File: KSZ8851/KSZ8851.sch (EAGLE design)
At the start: 53 parts, among them IC1 AT93C46A-10SQ-2.7, P1 RB1-125BAG1A

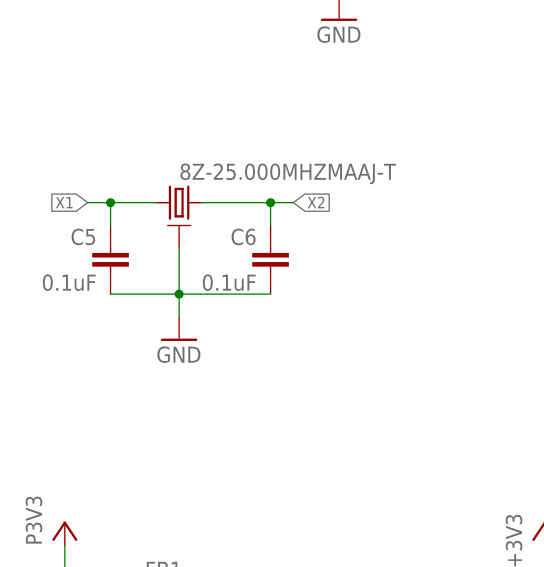
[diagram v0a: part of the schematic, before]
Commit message: Fix angle wire angle and add power LED
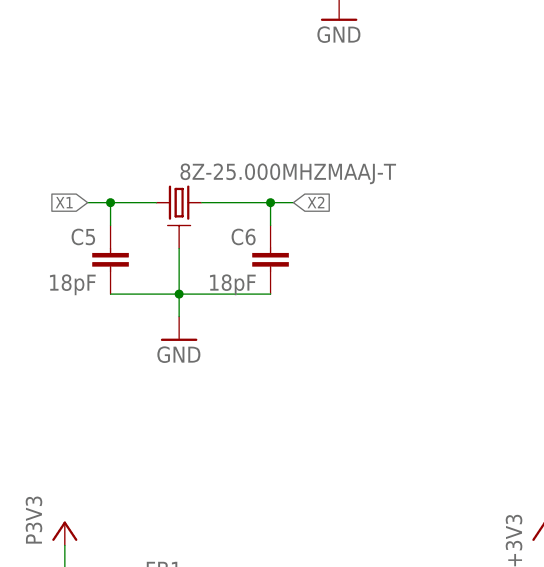
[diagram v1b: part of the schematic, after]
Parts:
- C5, C6: value 0.1uF -> 18pF
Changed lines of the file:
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@@
 <part name="+3V5" library="supply1" deviceset="+3V3" device=""/>
 <part name="-25.000MHZMAAJ-T1" library="crystal" deviceset="8Z" device="" technology="-25.000MHZMAAJ-T"/>
-<part name="C5" library="rcl" deviceset="C-EU" device="C0603" value="0.1uF"/>
-<part name="C6" library="rcl" deviceset="C-EU" device="C0603" value="0.1uF"/>
+<part name="C5" library="rcl" deviceset="C-EU" device="C0603" value="18pF"/>
+<part name="C6" library="rcl" deviceset="C-EU" device="C0603" value="18pF"/>
 <part name="GND7" library="supply1" deviceset="GND" device=""/>
 <part name="JP1" library="pinhead" deviceset="PINHD-2X5" device=""/>

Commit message: Generate gerber file
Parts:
- added LED1: Green, led:LEDSML0603
- added R13: 1.5k, rcl:R-EU_R0603
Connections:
- new net N$4: LED1.A, R13.2
- net +3V3: now also R13.1
- net GND: now also LED1.C
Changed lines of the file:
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@@
 <part name="SJ4" library="jumper" deviceset="SJ" device=""/>
 <part name="GND15" library="supply1" deviceset="GND" device=""/>
+<part name="LED1" library="led" deviceset="LED" device="SML0603" value="Green"/>
+<part name="R13" library="rcl" deviceset="R-EU_" device="R0603" value="1.5k"/>
 </parts>
 <sheets>
@@
 <instance part="SJ4" gate="1" x="342.9" y="43.18" rot="R90"/>
 <instance part="GND15" gate="1" x="335.28" y="48.26"/>
+<instance part="LED1" gate="G$1" x="76.2" y="96.52"/>
+<instance part="R13" gate="G$1" x="76.2" y="106.68" rot="R270"/>
 </instances>
 <busses>
@@
 <wire x1="66.04" y1="93.98" x2="66.04" y2="91.44" width="0.1524" layer="91"/>
 <junction x="66.04" y="93.98"/>
+<pinref part="LED1" gate="G$1" pin="C"/>
+<wire x1="76.2" y1="91.44" x2="66.04" y2="91.44" width="0.1524" layer="91"/>
+<junction x="66.04" y="91.44"/>
 </segment>
 <segment>
@@
 <wire x1="40.64" y1="109.22" x2="55.88" y2="109.22" width="0.1524" layer="91"/>
 <wire x1="55.88" y1="109.22" x2="66.04" y2="109.22" width="0.1524" layer="91"/>
-<wire x1="66.04" y1="109.22" x2="66.04" y2="114.3" width="0.1524" layer="91"/>
+<wire x1="66.04" y1="109.22" x2="66.04" y2="111.76" width="0.1524" layer="91"/>
 <pinref part="C10" gate="G$1" pin="1"/>
+<wire x1="66.04" y1="111.76" x2="66.04" y2="114.3" width="0.1524" layer="91"/>
 <wire x1="66.04" y1="101.6" x2="66.04" y2="109.22" width="0.1524" layer="91"/>
 <junction x="66.04" y="109.22"/>
@@
 <wire x1="40.64" y1="101.6" x2="40.64" y2="109.22" width="0.1524" layer="91"/>
 <junction x="40.64" y="109.22"/>
+<pinref part="R13" gate="G$1" pin="1"/>
+<wire x1="66.04" y1="111.76" x2="76.2" y2="111.76" width="0.1524" layer="91"/>
+<junction x="66.04" y="111.76"/>
 </segment>
 </net>
@@
 </segment>
 </net>
+<net name="N$4" class="0">
+<segment>
+<pinref part="R13" gate="G$1" pin="2"/>
+<pinref part="LED1" gate="G$1" pin="A"/>
+<wire x1="76.2" y1="101.6" x2="76.2" y2="99.06" width="0.1524" layer="91"/>
+</segment>
+</net>

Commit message: Add Exmachina logo and CC
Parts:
- added U$2: EXMACHINA-LOGO-NAME, exmachina:EXMACHINA-LOGO-NAME
- added U$3: CC-BY-SA, cc-by-sa:CC-BY-SA
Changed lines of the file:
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@@
 <part name="LED1" library="led" deviceset="LED" device="SML0603" value="Green"/>
 <part name="R13" library="rcl" deviceset="R-EU_" device="R0603" value="1.5k"/>
+<part name="U$2" library="exmachina" deviceset="EXMACHINA-LOGO" device="-NAME"/>
+<part name="U$3" library="cc-by-sa" deviceset="CC-BY-SA" device=""/>
 </parts>
 <sheets>
@@
 <instance part="LED1" gate="G$1" x="76.2" y="96.52"/>
 <instance part="R13" gate="G$1" x="76.2" y="106.68" rot="R270"/>
+<instance part="U$2" gate="G$1" x="311.15" y="19.05"/>
+<instance part="U$3" gate="A" x="303.53" y="8.89"/>
 </instances>
 <busses>

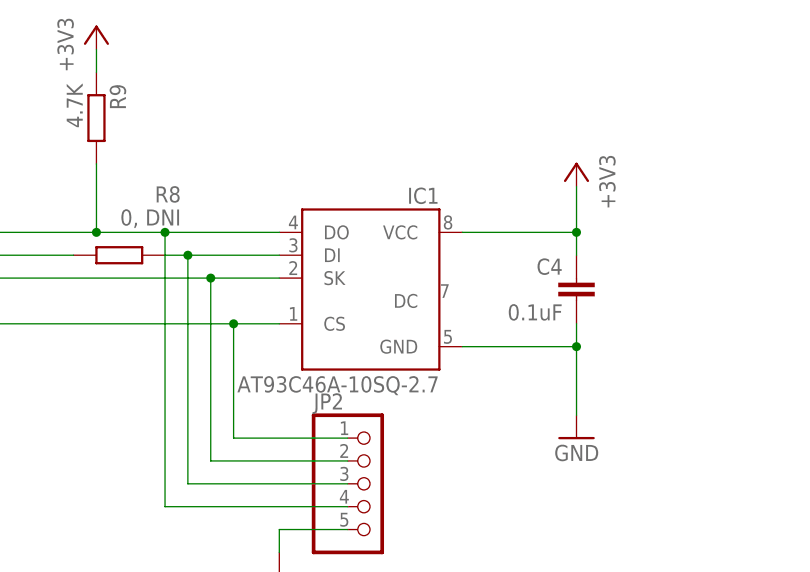
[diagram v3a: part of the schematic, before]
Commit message: Add BOM to KSZ8851 board and place component name on the board
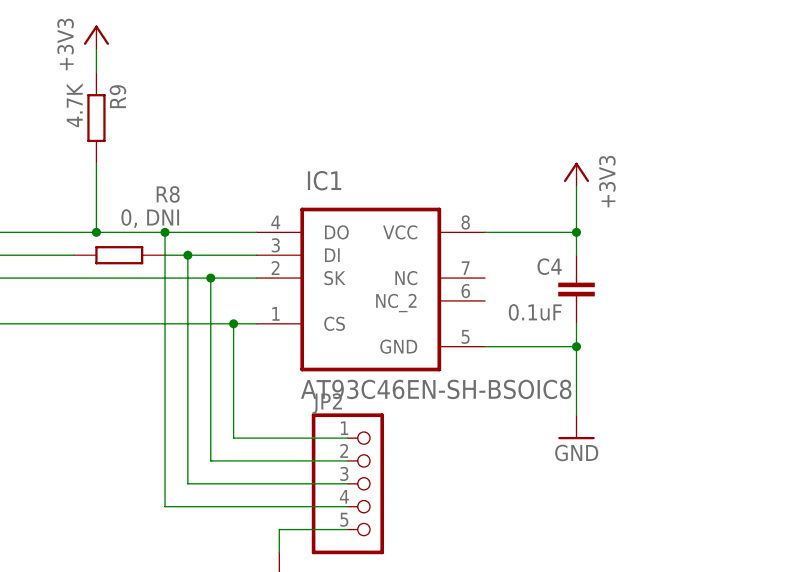
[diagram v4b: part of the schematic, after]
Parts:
- -25.000MHZMAAJ-T1: MPN (none) -> 8Z-25.000MAAJ-T; OC_NEWARK (none) -> 84R5794
- C1, C10, C13, C14, C2, C4, C9: MPN (none) -> MC0603B104K160CT; OC_NEWARK (none) -> 06R4923
- C11, C12, C3, C7, C8: MPN (none) -> MCCTA475M010; OC_NEWARK (none) -> 01M8221
- C5, C6: MPN (none) -> MC0603N180J500CT; OC_NEWARK (none) -> 06R5138
- FB1, FB2: OC_NEWARK (none) -> 66W8861
- IC1: value AT93C46A-10SQ-2.7 -> AT93C46EN-SH-BSOIC8; device atmel:AT93C46A-10SQ-2.7 -> atmel:AT93C46EN-SH-BSOIC8; MPN (none) -> AT93C46EN-SH-T; OC_NEWARK (none) -> 68T5247
- JP1: MPN (none) -> M20-9980546; OC_NEWARK (none) -> 84K8708
- JP2: MF (none) -> FARNELL; MPN (none) -> M22-2010505; OC_NEWARK (none) -> 08WX6673
- JP3, JP4, JP5, JP6, MP1, MP2, MP3, MP4, P1, SJ1, SJ2, SJ3, SJ4, TP1, TP2, TP3, TP4, TP5, TP6, TP7, U$2, U$3: OC_NEWARK (none) -> unknown
- LED1: MPN (none) -> OVS-0604; OC_NEWARK (none) -> 15R2206
- R1: MPN (none) -> MC0063W060313K01; OC_NEWARK (none) -> 94W5780
- R10, R11, R12, R9: MF (none) -> Multicomp Passives; MPN (none) -> MC0063W060314K7; OC_NEWARK (none) -> 58K4608
- R13: MPN (none) -> MCMR06X1501FTL; OC_NEWARK (none) -> 86T3542
- R2, R3, R4, R5: MPN (none) -> MC0603SAF499JT5E; OC_NEWARK (none) -> 79M5983
- R6, R7: MF (none) -> Multicomp Passives; MPN (none) -> MC0063W06031220R; OC_NEWARK (none) -> 58K4526
- R8: MF (none) -> Multicomp Passives; MPN (none) -> MC0603WG00000T5E-TC; OC_NEWARK (none) -> 58K4684
- U$1: MPN (none) -> KSZ8851SNLI-TR; OC_NEWARK (none) -> 72Y5310
